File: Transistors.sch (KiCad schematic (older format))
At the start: 0 parts

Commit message: Connected hierarchical labels in Top.sch Beautified label order in Transistors.sch
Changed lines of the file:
@@
 $Descr A4 11693 8268
 encoding utf-8
-Sheet 3 10
+Sheet 5 10
 Title ""
 Date ""
@@
 Comment4 ""
 $EndDescr
+Text HLabel 2650 1800 0    60   Input ~ 0
+T1_Input_1
 Text HLabel 2650 1900 0    60   Input ~ 0
 T1_Enable_A
@@
 Text HLabel 2650 4500 0    60   Input ~ 0
 T2_Input_4
+Text HLabel 4450 3950 2    60   Output ~ 0
+T2_Output_1
+Text HLabel 4450 4050 2    60   Output ~ 0
+T2_Output_2
+Text HLabel 4450 4350 2    60   Output ~ 0
+T2_Output_3
+Text HLabel 4450 4450 2    60   Output ~ 0
+T2_Output_4
 Wire Wire Line
 	2650 3900 2950 3900
@@
 Text HLabel 2650 6600 0    60   Input ~ 0
 T3_Input_4
-Wire Wire Line
-	2650 6000 2950 6000
-Wire Wire Line
-	2650 6100 2950 6100
-Wire Wire Line
-	2650 6200 2950 6200
-Wire Wire Line
-	2650 6400 2950 6400
-Wire Wire Line
-	2650 6500 2950 6500
-Wire Wire Line
-	2650 6600 2950 6600
-Text HLabel 4450 3950 2    60   Output ~ 0
-T2_Output_1
-Text HLabel 4450 4050 2    60   Output ~ 0
-T2_Output_2
-Text HLabel 4450 4350 2    60   Output ~ 0
-T2_Output_3
-Text HLabel 4450 4450 2    60   Output ~ 0
-T2_Output_4
-Wire Wire Line
-	4200 3950 4450 3950
-Wire Wire Line
-	4200 4050 4450 4050
-Wire Wire Line
-	4200 4350 4450 4350
-Wire Wire Line
-	4200 4450 4450 4450
 Text HLabel 4450 6050 2    60   Output ~ 0
 T3_Output_1
@@
 T3_Output_4
 Wire Wire Line
+	2650 6000 2950 6000
+Wire Wire Line
+	2650 6100 2950 6100
+Wire Wire Line
+	2650 6200 2950 6200
+Wire Wire Line
+	2650 6400 2950 6400
+Wire Wire Line
+	2650 6500 2950 6500
+Wire Wire Line
+	2650 6600 2950 6600
+Wire Wire Line
+	4200 3950 4450 3950
+Wire Wire Line
+	4200 4050 4450 4050
+Wire Wire Line
+	4200 4350 4450 4350
+Wire Wire Line
+	4200 4450 4450 4450
+Wire Wire Line
 	4200 6050 4450 6050
 Wire Wire Line
@@
 Wire Wire Line
 	4200 6550 4450 6550
-Text HLabel 8900 1950 2    60   Output ~ 0
-T4_Output_1
-Text HLabel 8900 2050 2    60   Output ~ 0
-T4_Output_2
-Text HLabel 8900 2350 2    60   Output ~ 0
-T4_Output_3
-Text HLabel 8900 2450 2    60   Output ~ 0
-T4_Output_4
-Wire Wire Line
-	8650 1950 8900 1950
-Wire Wire Line
-	8650 2050 8900 2050
-Wire Wire Line
-	8650 2350 8900 2350
-Wire Wire Line
-	8650 2450 8900 2450
-Text HLabel 8900 4400 2    60   Input ~ 0
-T5_Output_3
-Wire Wire Line
-	8650 4000 8900 4000
-Wire Wire Line
-	8650 4100 8900 4100
-Wire Wire Line
-	8650 4400 8900 4400
-Wire Wire Line
-	8650 4500 8900 4500
 Text HLabel 7100 1900 0    60   Input ~ 0
 T4_Input_1
@@
 Text HLabel 7100 2500 0    60   Input ~ 0
 T4_Input_4
+Text HLabel 8900 1950 2    60   Output ~ 0
+T4_Output_1
+Text HLabel 8900 2050 2    60   Output ~ 0
+T4_Output_2
+Text HLabel 8900 2350 2    60   Output ~ 0
+T4_Output_3
+Text HLabel 8900 2450 2    60   Output ~ 0
+T4_Output_4
+Wire Wire Line
+	8650 1950 8900 1950
+Wire Wire Line
+	8650 2050 8900 2050
+Wire Wire Line
+	8650 2350 8900 2350
+Wire Wire Line
+	8650 2450 8900 2450
+Wire Wire Line
+	8650 4000 8900 4000
+Wire Wire Line
+	8650 4100 8900 4100
+Wire Wire Line
+	8650 4400 8900 4400
+Wire Wire Line
+	8650 4500 8900 4500
 Wire Wire Line
 	7100 1900 7400 1900
@@
 Text HLabel 7100 4550 0    60   Input ~ 0
 T5_Input_4
+Text HLabel 8900 4000 2    60   Output ~ 0
+T5_Output_1
+Text HLabel 8900 4100 2    60   Output ~ 0
+T5_Output_2
+Text HLabel 8900 4400 2    60   Output ~ 0
+T5_Output_3
+Text HLabel 8900 4500 2    60   Output ~ 0
+T5_Output_4
 Wire Wire Line
 	7100 3950 7400 3950
@@
 Wire Wire Line
 	7100 4550 7400 4550
-Text HLabel 2650 1800 0    60   Input ~ 0
-T1_Input_1
 $Sheet
 S 2950 1700 1250 800
@@
 F11 "Output_4" O R 4200 2350 60
 $EndSheet
-Text HLabel 8900 4000 2    60   Output ~ 0
-T5_Output_1
-Text HLabel 8900 4100 2    60   Output ~ 0
-T5_Output_2
-Text HLabel 8900 4500 2    60   Output ~ 0
-T5_Output_4
 $Sheet
 S 2950 3800 1250 800

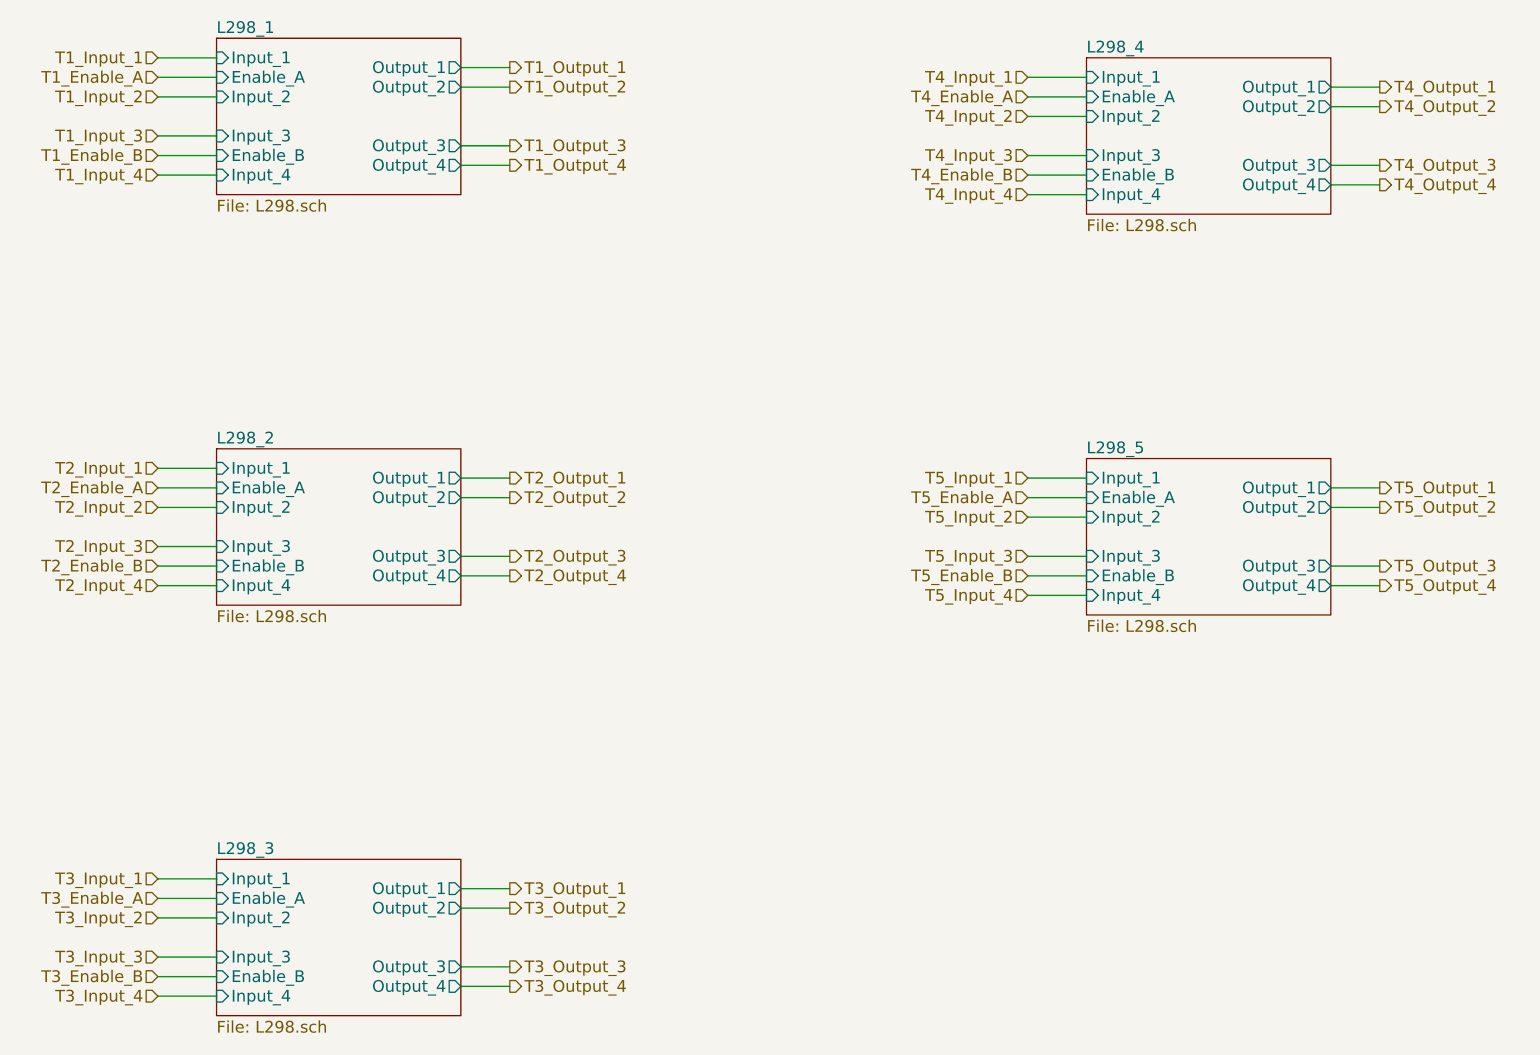
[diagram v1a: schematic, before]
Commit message: Added and connected sixth L298N symbol
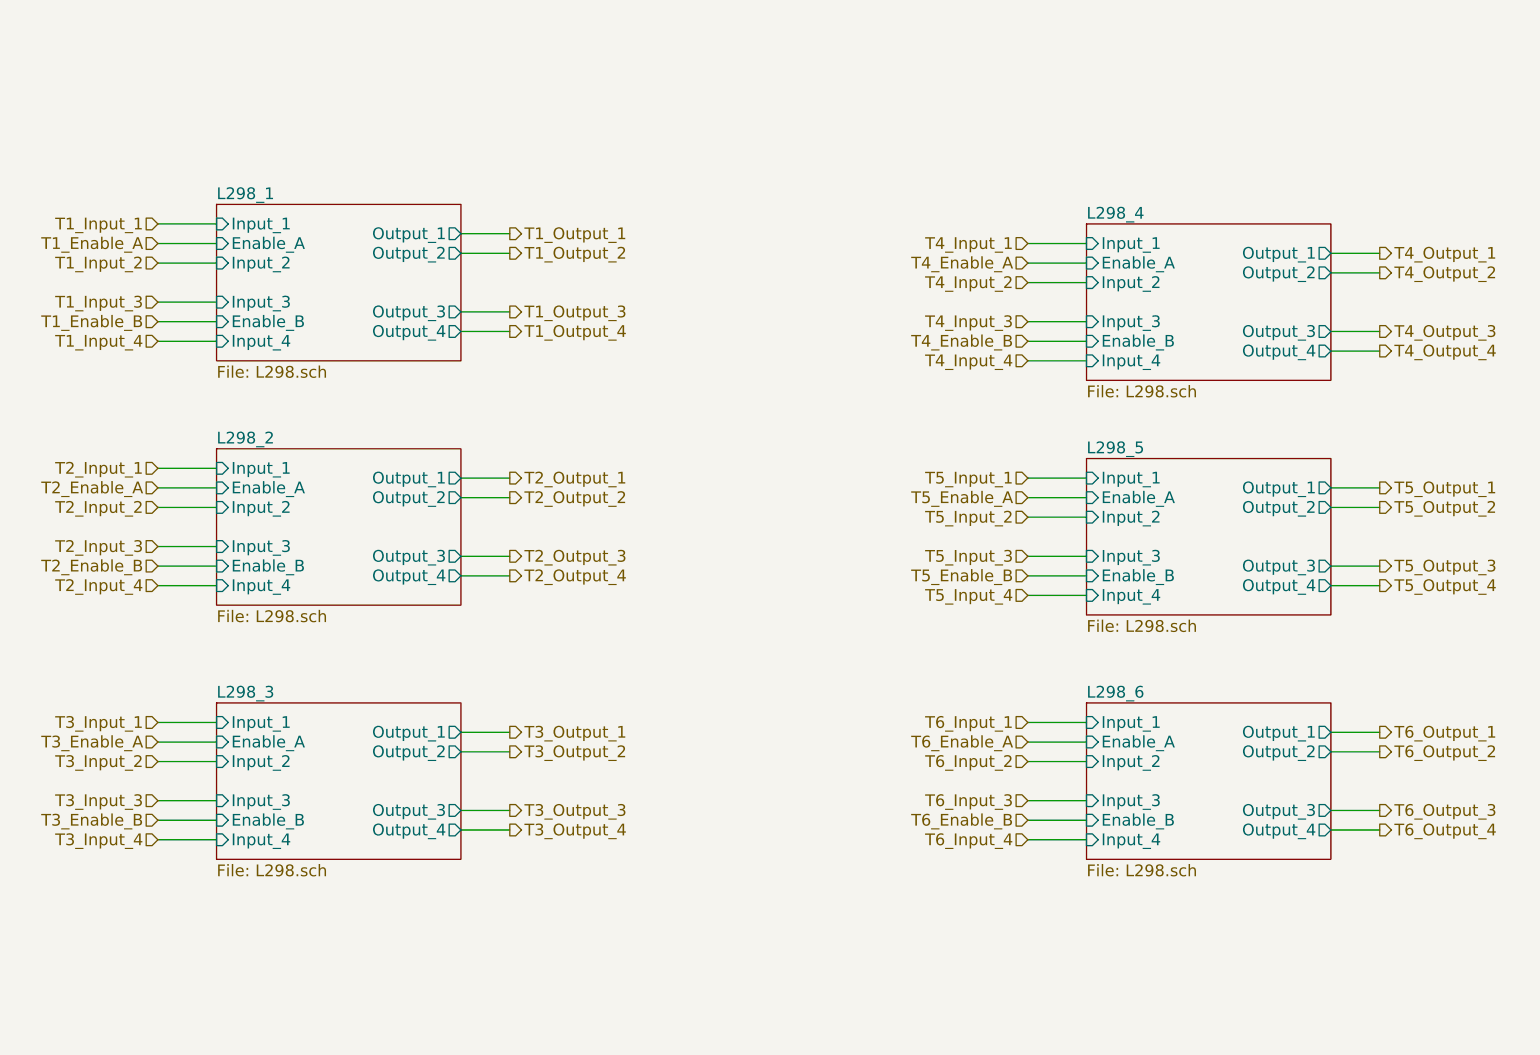
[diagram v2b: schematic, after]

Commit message: Added Chopper.sch
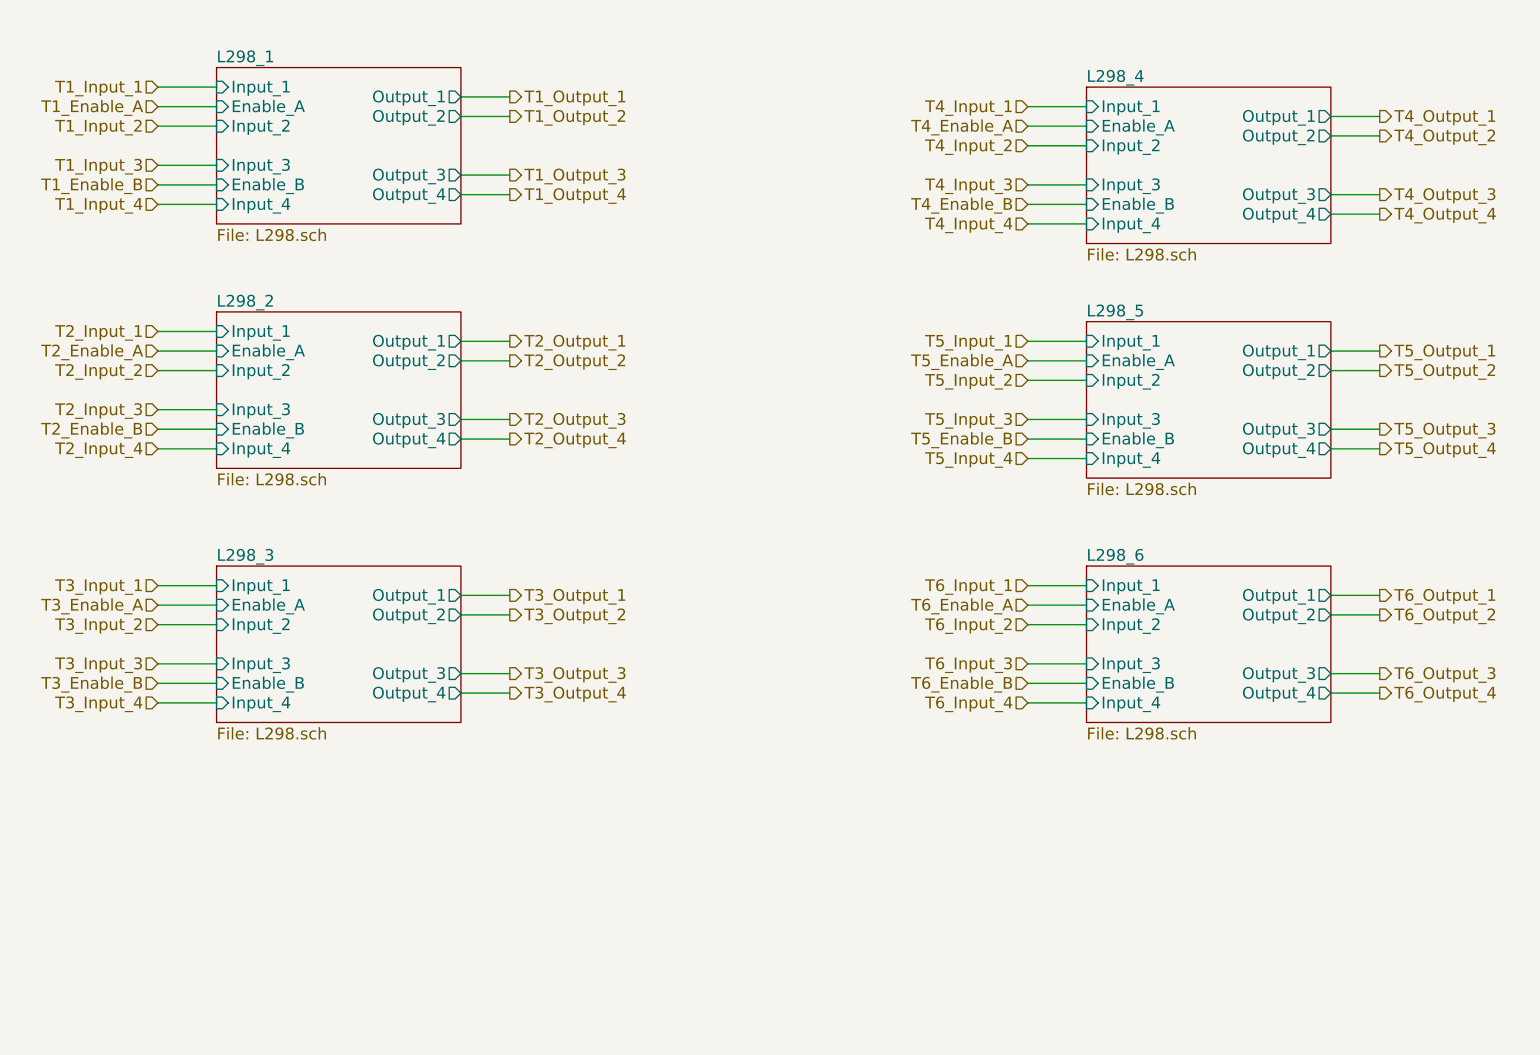
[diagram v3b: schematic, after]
